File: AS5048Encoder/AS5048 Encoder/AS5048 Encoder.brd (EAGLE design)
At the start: 47.8 x 50 mm, 5 parts, among them X1 SI-50170

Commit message: all parts in place
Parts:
- added TP1, TP2, TP3, TP4, TP5: TPPAD1-17, testpad:P1-17
- added U$2: AS5145, makesmith:SSOP16
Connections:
- new net N$10: X1.7
- new net N$11: X1.8
- new net N$2: U$2.11
- new net N$3: U$2.10
- new net N$4: U$2.9
- new net N$9: X1.6
- new net SIG_A: TP4.TP, U$2.3, X1.4
- new net SIG_B: TP5.TP, U$2.4, X1.5
- net GND: now also TP2.TP
- net PWM: now also TP3.TP, U$2.12
- net VCC: now also TP1.TP
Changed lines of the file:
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@@
 <attribute name="OC_NEWARK" value="unknown" x="25" y="6.4" size="1.778" layer="28" rot="MR0" display="off"/>
+</element>
+<element name="U$2" library="makesmith" package="SSOP16" value="AS5145" x="30.3784" y="46.1518"/>
+<element name="TP1" library="testpad" package="P1-17" value="TPPAD1-17" x="43.3832" y="18.1864">
+<attribute name="TP_SIGNAL_NAME" value="" x="43.3832" y="18.1864" size="1.778" layer="27" display="off"/>
+</element>
+<element name="TP2" library="testpad" package="P1-17" value="TPPAD1-17" x="3.0734" y="-15.0368">
+<attribute name="TP_SIGNAL_NAME" value="" x="3.0734" y="-15.0368" size="1.778" layer="27" display="off"/>
+</element>
+<element name="TP3" library="testpad" package="P1-17" value="TPPAD1-17" x="3.0734" y="-19.5072">
+<attribute name="TP_SIGNAL_NAME" value="" x="3.0734" y="-19.5072" size="1.778" layer="27" display="off"/>
+</element>
+<element name="TP4" library="testpad" package="P1-17" value="TPPAD1-17" x="3.0734" y="-23.9776">
+<attribute name="TP_SIGNAL_NAME" value="" x="3.0734" y="-23.9776" size="1.778" layer="27" display="off"/>
+</element>
+<element name="TP5" library="testpad" package="P1-17" value="TPPAD1-17" x="3.0734" y="-28.448">
+<attribute name="TP_SIGNAL_NAME" value="" x="3.0734" y="-28.448" size="1.778" layer="27" display="off"/>
 </element>
 </elements>
@@
 <wire x1="32.5882" y1="24.638" x2="32.5882" y2="22.267025" width="0.4064" layer="1"/>
 <wire x1="32.5882" y1="22.267025" x2="32.55431875" y2="22.23314375" width="0.4064" layer="1"/>
+<contactref element="TP2" pad="TP"/>
+<wire x1="3.0734" y1="-15.0368" x2="23.095" y2="12.242" width="0" layer="19" extent="1-1"/>
 </signal>
 <signal name="VCC">
@@
 <wire x1="35.1028" y1="26.2128" x2="35.1028" y2="21.987625" width="0.4064" layer="1"/>
 <wire x1="35.1028" y1="21.987625" x2="35.09431875" y2="21.97914375" width="0.4064" layer="1"/>
+<contactref element="TP1" pad="TP"/>
+<wire x1="35.1028" y1="21.987625" x2="43.3832" y2="18.1864" width="0" layer="19" extent="1-1"/>
 </signal>
 <signal name="3V3">
@@
 <wire x1="27.4828" y1="46.0248" x2="19.24021875" y2="46.0248" width="0.4064" layer="1"/>
 <wire x1="19.24021875" y1="46.0248" x2="19.21541875" y2="46" width="0.4064" layer="1"/>
+<contactref element="U$2" pad="12"/>
+<contactref element="TP3" pad="TP"/>
+<wire x1="27.4828" y1="46.0248" x2="34.8884" y2="45.8268" width="0" layer="19" extent="1-1"/>
+<wire x1="3.0734" y1="-19.5072" x2="24.227" y2="7.3" width="0" layer="19" extent="1-1"/>
+</signal>
+<signal name="N$2">
+<contactref element="U$2" pad="11"/>
+</signal>
+<signal name="N$3">
+<contactref element="U$2" pad="10"/>
+</signal>
+<signal name="N$4">
+<contactref element="U$2" pad="9"/>
+</signal>
+<signal name="SIG_A">
+<contactref element="U$2" pad="3"/>
+<contactref element="X1" pad="4"/>
+<contactref element="TP4" pad="TP"/>
+<wire x1="24.365" y1="9.702" x2="25.8684" y2="47.1268" width="0" layer="19" extent="1-1"/>
+<wire x1="3.0734" y1="-23.9776" x2="24.365" y2="9.702" width="0" layer="19" extent="1-1"/>
+</signal>
+<signal name="SIG_B">
+<contactref element="U$2" pad="4"/>
+<contactref element="X1" pad="5"/>
+<contactref element="TP5" pad="TP"/>
+<wire x1="25.635" y1="12.242" x2="25.8684" y2="46.4768" width="0" layer="19" extent="1-1"/>
+<wire x1="3.0734" y1="-28.448" x2="25.635" y2="12.242" width="0" layer="19" extent="1-1"/>
+</signal>
+<signal name="N$9">
+<contactref element="X1" pad="6"/>
+</signal>
+<signal name="N$10">
+<contactref element="X1" pad="7"/>
+</signal>
+<signal name="N$11">
+<contactref element="X1" pad="8"/>
 </signal>
 </signals>

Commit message: board looks done?
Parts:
- removed U$1: AS5048, austriamicrosystems:TSOP14
- moved TP3 60.8 mm to (37.7, 30.4)
- moved TP5 55.0 mm to (12.4, 25.7)
- moved TP4 50.2 mm to (7.98, 25.9)
- moved TP2 48.7 mm to (28.2, 26.6)
- moved TP1 17.5 mm to (32.4, 31.9)
- moved U$2 14.4 mm to (16.1, 44.0)
- moved C3 4.24 mm to (16.2, 36.1)
- moved C4 2.51 mm to (19.3, 36.1)
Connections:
- removed net N$10: X1.7
- removed net N$11: X1.8
- removed net N$9: X1.6
- net 3V3: now also U$2.15; no longer U$1.12
- net GND: now also X1.7; no longer U$1.13, X1.3
- net PWM: now also X1.8; no longer U$1.14, X1.2
- net SIG_A: now also X1.2; no longer X1.4
- net SIG_B: now also X1.1; no longer X1.5
- net VCC: now also U$2.16, X1.6; no longer U$1.11, X1.1
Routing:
- net SIG_A: track 0.00 -> 47.3 mm
- net SIG_B: track 0.00 -> 39.4 mm
- net GND: track 51.9 -> 33.2 mm
- net PWM: track 63.2 -> 46.8 mm
- net VCC: track 52.3 -> 58.1 mm
- net 3V3: track 8.41 -> 10.5 mm
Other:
- outline, holes or cut-outs redrawn

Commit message: routed mode
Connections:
- new net MODE_INDEX: U$2.6, X1.3
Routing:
- net MODE_INDEX: track 0.00 -> 40.2 mm
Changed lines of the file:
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@@
 <dimension x1="10" y1="10" x2="25" y2="44" x3="25.0444" y3="27" textsize="1.778" layer="22" dtype="vertical"/>
 <dimension x1="10" y1="10" x2="16.15" y2="44" x3="13.075" y3="20.4216" textsize="1.778" layer="22" dtype="horizontal"/>
+<circle x="16.129" y="44.0182" radius="0.993525" width="0.4064" layer="22"/>
 </plain>
 <attributes>
@@
 <wire x1="12.4206" y1="20.3764" x2="12.4206" y2="25.7302" width="0.4064" layer="1"/>
 </signal>
+<signal name="MODE_INDEX">
+<contactref element="U$2" pad="6"/>
+<contactref element="X1" pad="3"/>
+<wire x1="11.64" y1="43.025" x2="11.6882" y2="42.9768" width="0.4064" layer="1"/>
+<wire x1="11.6882" y1="42.9768" x2="14.2494" y2="42.9768" width="0.4064" layer="1"/>
+<wire x1="14.2494" y1="42.9768" x2="14.9606" y2="42.2656" width="0.4064" layer="1"/>
+<wire x1="14.9606" y1="42.2656" x2="14.9606" y2="40.7162" width="0.4064" layer="1"/>
+<wire x1="14.9606" y1="40.7162" x2="12.3698" y2="38.1254" width="0.4064" layer="1"/>
+<wire x1="12.3698" y1="38.1254" x2="12.3698" y2="30.7594" width="0.4064" layer="1"/>
+<wire x1="12.3698" y1="30.7594" x2="24.384" y2="18.7452" width="0.4064" layer="1"/>
+<wire x1="24.384" y1="18.7452" x2="24.384" y2="15.113" width="0.4064" layer="1"/>
+<wire x1="24.384" y1="15.113" x2="23.095" y2="13.824" width="0.4064" layer="1"/>
+<wire x1="23.095" y1="13.824" x2="23.095" y2="12.242" width="0.4064" layer="1"/>
+</signal>
 </signals>

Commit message: added ground connection
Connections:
- net GND: now also U$2.7
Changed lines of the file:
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@@
 <wire x1="20.37058125" y1="34.41688125" x2="32.55431875" y2="22.23314375" width="0.4064" layer="1"/>
 <contactref element="X1" pad="7"/>
-<wire x1="32.55431875" y1="22.23314375" x2="28.2194" y2="26.6446" width="0" layer="19" extent="1-1"/>
 <wire x1="28.175" y1="12.242" x2="32.55431875" y2="16.62131875" width="0.4064" layer="1"/>
 <wire x1="32.55431875" y1="16.62131875" x2="32.55431875" y2="22.23314375" width="0.4064" layer="1"/>
+<contactref element="U$2" pad="7"/>
+<wire x1="32.55431875" y1="22.23314375" x2="28.2194" y2="26.6446" width="0" layer="19" extent="1-1"/>
+<wire x1="11.64" y1="42.375" x2="16.2044625" y2="34.412221875" width="0" layer="19" extent="1-1"/>
 </signal>
 <signal name="VCC">

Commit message: cns low
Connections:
- removed net N$2: U$2.11
- net GND: now also U$2.11
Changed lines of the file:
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@@
 <wire x1="32.55431875" y1="16.62131875" x2="32.55431875" y2="22.23314375" width="0.4064" layer="1"/>
 <contactref element="U$2" pad="7"/>
-<wire x1="32.55431875" y1="22.23314375" x2="28.2194" y2="26.6446" width="0" layer="19" extent="1-1"/>
-<wire x1="11.64" y1="42.375" x2="16.2044625" y2="34.412221875" width="0" layer="19" extent="1-1"/>
+<contactref element="U$2" pad="11"/>
+<wire x1="20.37058125" y1="34.41688125" x2="20.66" y2="43.025" width="0" layer="19" extent="1-1"/>
+<wire x1="28.2194" y1="26.6446" x2="32.55431875" y2="22.23314375" width="0" layer="19" extent="1-1"/>
+<wire x1="11.64" y1="42.375" x2="20.66" y2="43.025" width="0" layer="19" extent="1-1"/>
 </signal>
 <signal name="VCC">
@@
 <wire x1="37.63431875" y1="17.89131875" x2="37.63431875" y2="22.23314375" width="0.4064" layer="1"/>
 </signal>
-<signal name="N$2">
-<contactref element="U$2" pad="11"/>
-</signal>
 <signal name="N$3">

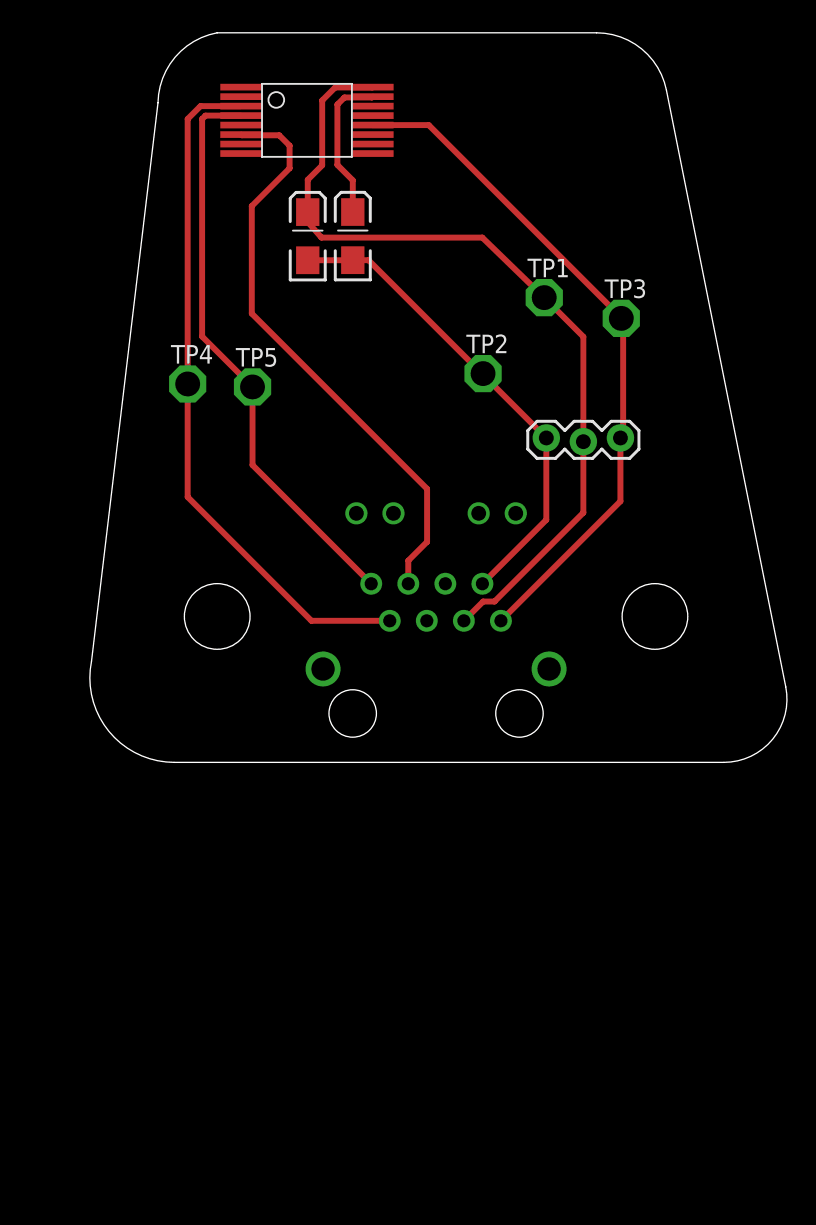
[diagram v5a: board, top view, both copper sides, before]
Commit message: total revamp of encoder board
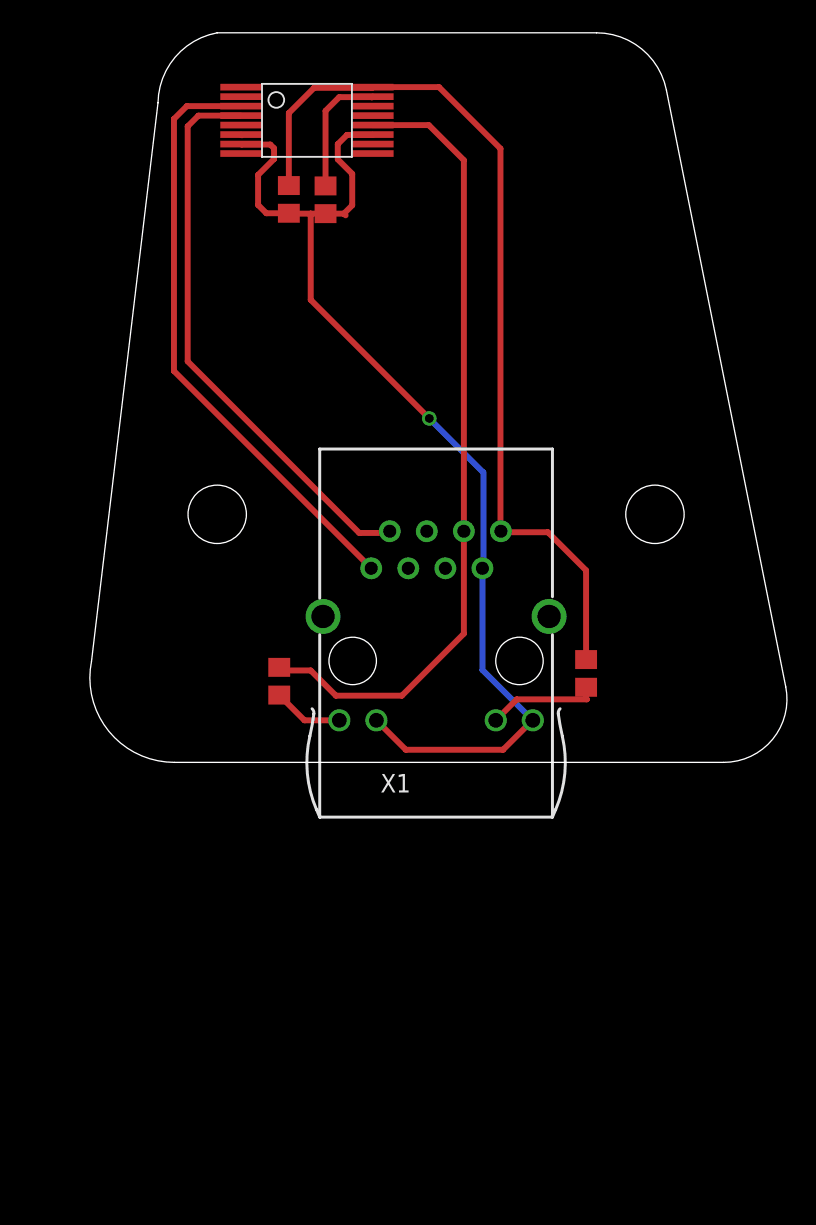
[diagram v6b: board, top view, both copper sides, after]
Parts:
- removed C3: 100nF, SparkFun-Passives:EIA3216-KIT
- removed C4: 10uF, SparkFun-Passives:EIA3216-KIT
- removed JP1: (no value), SparkFun-Connectors:1X03_LOCK
- removed TP1, TP2, TP3, TP4, TP5: TPPAD1-17, testpad:P1-17
- added C1: 100nF, eagle-ltspice:C0805
- added C2: 10uF, eagle-ltspice:C0805
- added R1, R2: 270, eagle-ltspice:R0805
- moved X1 3.60 mm to (25.0, 10.0), flipped to the top
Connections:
- new net LED1: R1.1, X1.A1
- new net LED2: R2.1, X1.A2
- net 3V3: now also C2.1; no longer C4.A
- net GND: now also C1.2, C2.2, X1.2, X1.C1, X1.C2; no longer C3.C, C4.C, JP1.1, TP2.TP, X1.7
- net MODE_INDEX: no longer X1.3
- net PWM: now also R1.2, X1.3; no longer JP1.3, TP3.TP, X1.8
- net SIG_A: now also X1.8; no longer TP4.TP, X1.2
- net SIG_B: now also X1.7; no longer TP5.TP, X1.1
- net VCC: now also C1.1, R2.2, X1.1; no longer C3.A, JP1.2, TP1.TP, X1.6
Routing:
- net GND: track 33.2 -> 74.6 mm, vias 0 -> 1
- net MODE_INDEX: track 40.2 -> 0.07 mm
- net PWM: track 46.8 -> 54.9 mm
- net LED2: track 0.00 -> 7.69 mm
- net SIG_A: track 47.3 -> 41.4 mm
- net LED1: track 0.00 -> 4.84 mm
- net VCC: track 58.1 -> 61.3 mm
- net 3V3: track 10.5 -> 8.87 mm
- net SIG_B: track 39.4 -> 38.8 mm

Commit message: reroute and move around
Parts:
- added SV1: (no value), con-lstb:MA03-1
- added U$1: TERMINALBLOCK277-1667-ND, makesmith:TERMINALBLOCK277-1667-ND
- moved R1 31.5 mm to (9.53, 36.8), turned to 0 degrees
- moved X1 21.7 mm to (11.0, 26.6), turned to 270 degrees
- moved R2 21.2 mm to (17.0, 16.8), turned to 0 degrees
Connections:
- new net PWR: SV1.2, U$1.2
- new net SERVO: SV1.1, X1.5
- net GND: now also SV1.3, U$1.1
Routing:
- net GND: track 74.6 -> 96.0 mm
- net PWR: track 0.00 -> 18.2 mm
- net SERVO: track 0.00 -> 17.6 mm
- net LED2: track 7.69 -> 15.9 mm
- net VCC: track 61.3 -> 56.9 mm
- net PWM: track 54.9 -> 51.4 mm
- net SIG_B: track 38.8 -> 40.9 mm, vias 0 -> 1
- net LED1: track 4.84 -> 6.20 mm
- net SIG_A: track 41.4 -> 41.1 mm, vias 0 -> 1
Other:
- board size 47.8 x 50 mm -> 35 x 45.1 mm

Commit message: shipped here
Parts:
- moved R1 0.86 mm to (9.53, 37.6)
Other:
- outline, holes or cut-outs redrawn
- board text added: "+"
- board text added: "-"
- board text added: "GND"
- board text added: "PWM"
- board text added: "VCC"
